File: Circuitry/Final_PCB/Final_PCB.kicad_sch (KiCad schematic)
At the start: 84 parts

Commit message: vacuum converter
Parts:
- C1, C2, C3, C4, C7: footprint Resistor_THT:R_Axial_DIN0204_L3.6mm_D1.6mm_P7.62mm_Horizontal -> Capacitor_THT:CP_Radial_D4.0mm_P2.00mm
- C5, C6: footprint Resistor_THT:R_Axial_DIN0207_L6.3mm_D2.5mm_P7.62mm_Horizontal -> Capacitor_THT:CP_Radial_D4.0mm_P2.00mm
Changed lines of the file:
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@@
       (effects (font (size 1.27 1.27)) (justify left) hide)
     )
-    (property "Footprint" "Resistor_THT:R_Axial_DIN0204_L3.6mm_D1.6mm_P7.62mm_Horizontal" (at 376.8852 172.72 0)
+    (property "Footprint" "Capacitor_THT:CP_Radial_D4.0mm_P2.00mm" (at 376.8852 172.72 0)
       (effects (font (size 1.27 1.27)) hide)
     )
@@
       (effects (font (size 1.27 1.27)) (justify left) hide)
     )
-    (property "Footprint" "Resistor_THT:R_Axial_DIN0204_L3.6mm_D1.6mm_P7.62mm_Horizontal" (at 378.1552 130.81 0)
+    (property "Footprint" "Capacitor_THT:CP_Radial_D4.0mm_P2.00mm" (at 378.1552 130.81 0)
       (effects (font (size 1.27 1.27)) hide)
     )
@@
       (effects (font (size 1.27 1.27)) (justify left) hide)
     )
-    (property "Footprint" "Resistor_THT:R_Axial_DIN0207_L6.3mm_D2.5mm_P7.62mm_Horizontal" (at 392.1252 172.72 0)
+    (property "Footprint" "Capacitor_THT:CP_Radial_D4.0mm_P2.00mm" (at 392.1252 172.72 0)
       (effects (font (size 1.27 1.27)) hide)
     )
@@
       (effects (font (size 1.27 1.27)) (justify left) hide)
     )
-    (property "Footprint" "Resistor_THT:R_Axial_DIN0207_L6.3mm_D2.5mm_P7.62mm_Horizontal" (at 408.6352 172.72 0)
+    (property "Footprint" "Capacitor_THT:CP_Radial_D4.0mm_P2.00mm" (at 408.6352 172.72 0)
       (effects (font (size 1.27 1.27)) hide)
     )
@@
       (effects (font (size 1.27 1.27)) (justify left) hide)
     )
-    (property "Footprint" "Resistor_THT:R_Axial_DIN0204_L3.6mm_D1.6mm_P7.62mm_Horizontal" (at 409.9052 130.81 0)
+    (property "Footprint" "Capacitor_THT:CP_Radial_D4.0mm_P2.00mm" (at 409.9052 130.81 0)
       (effects (font (size 1.27 1.27)) hide)
     )
@@
       (effects (font (size 1.27 1.27)) (justify left) hide)
     )
-    (property "Footprint" "Resistor_THT:R_Axial_DIN0204_L3.6mm_D1.6mm_P7.62mm_Horizontal" (at 393.3952 130.81 0)
+    (property "Footprint" "Capacitor_THT:CP_Radial_D4.0mm_P2.00mm" (at 393.3952 130.81 0)
       (effects (font (size 1.27 1.27)) hide)
     )
@@
     (in_bom yes) (on_board yes) (dnp no) (fields_autoplaced)
     (property "Reference" "C7" (at 396.24 212.09 0)
-      (effects (font (size 1.27 1.27)) (justify left))
+      (effects (font (size 1.27 1.27)) (justify left) hide)
     )
     (property "Value" "47 uF" (at 396.24 214.63 0)
-      (effects (font (size 1.27 1.27)) (justify left) hide)
-    )
-    (property "Footprint" "Resistor_THT:R_Axial_DIN0204_L3.6mm_D1.6mm_P7.62mm_Horizontal" (at 393.3952 217.17 0)
-      (effects (font (size 1.27 1.27)) hide)
-    )
+      (effects (font (size 1.27 1.27)) (justify left))
+    )
+    (property "Footprint" "Capacitor_THT:CP_Radial_D4.0mm_P2.00mm" (at 393.3952 217.17 0)
+      (effects (font (size 1.27 1.27)) hide)
+    )

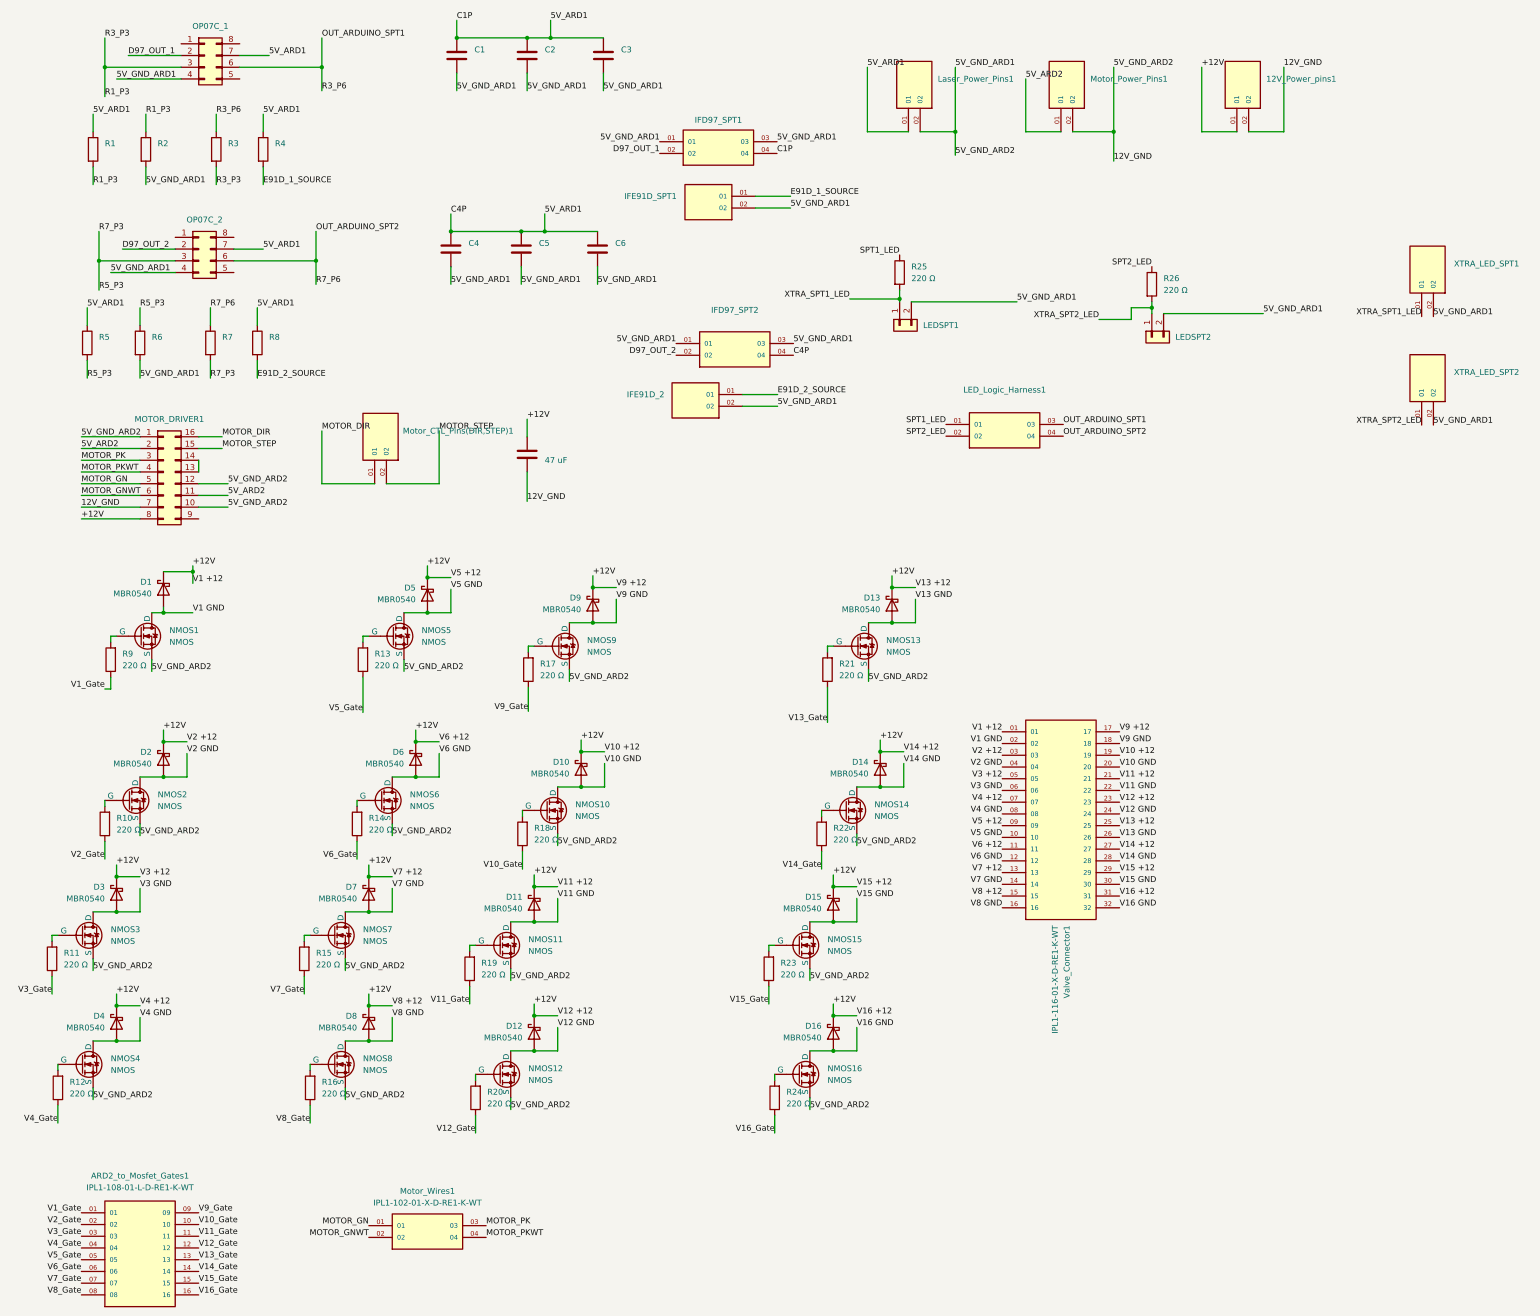
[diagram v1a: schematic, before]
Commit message: PCB minor correction/revision
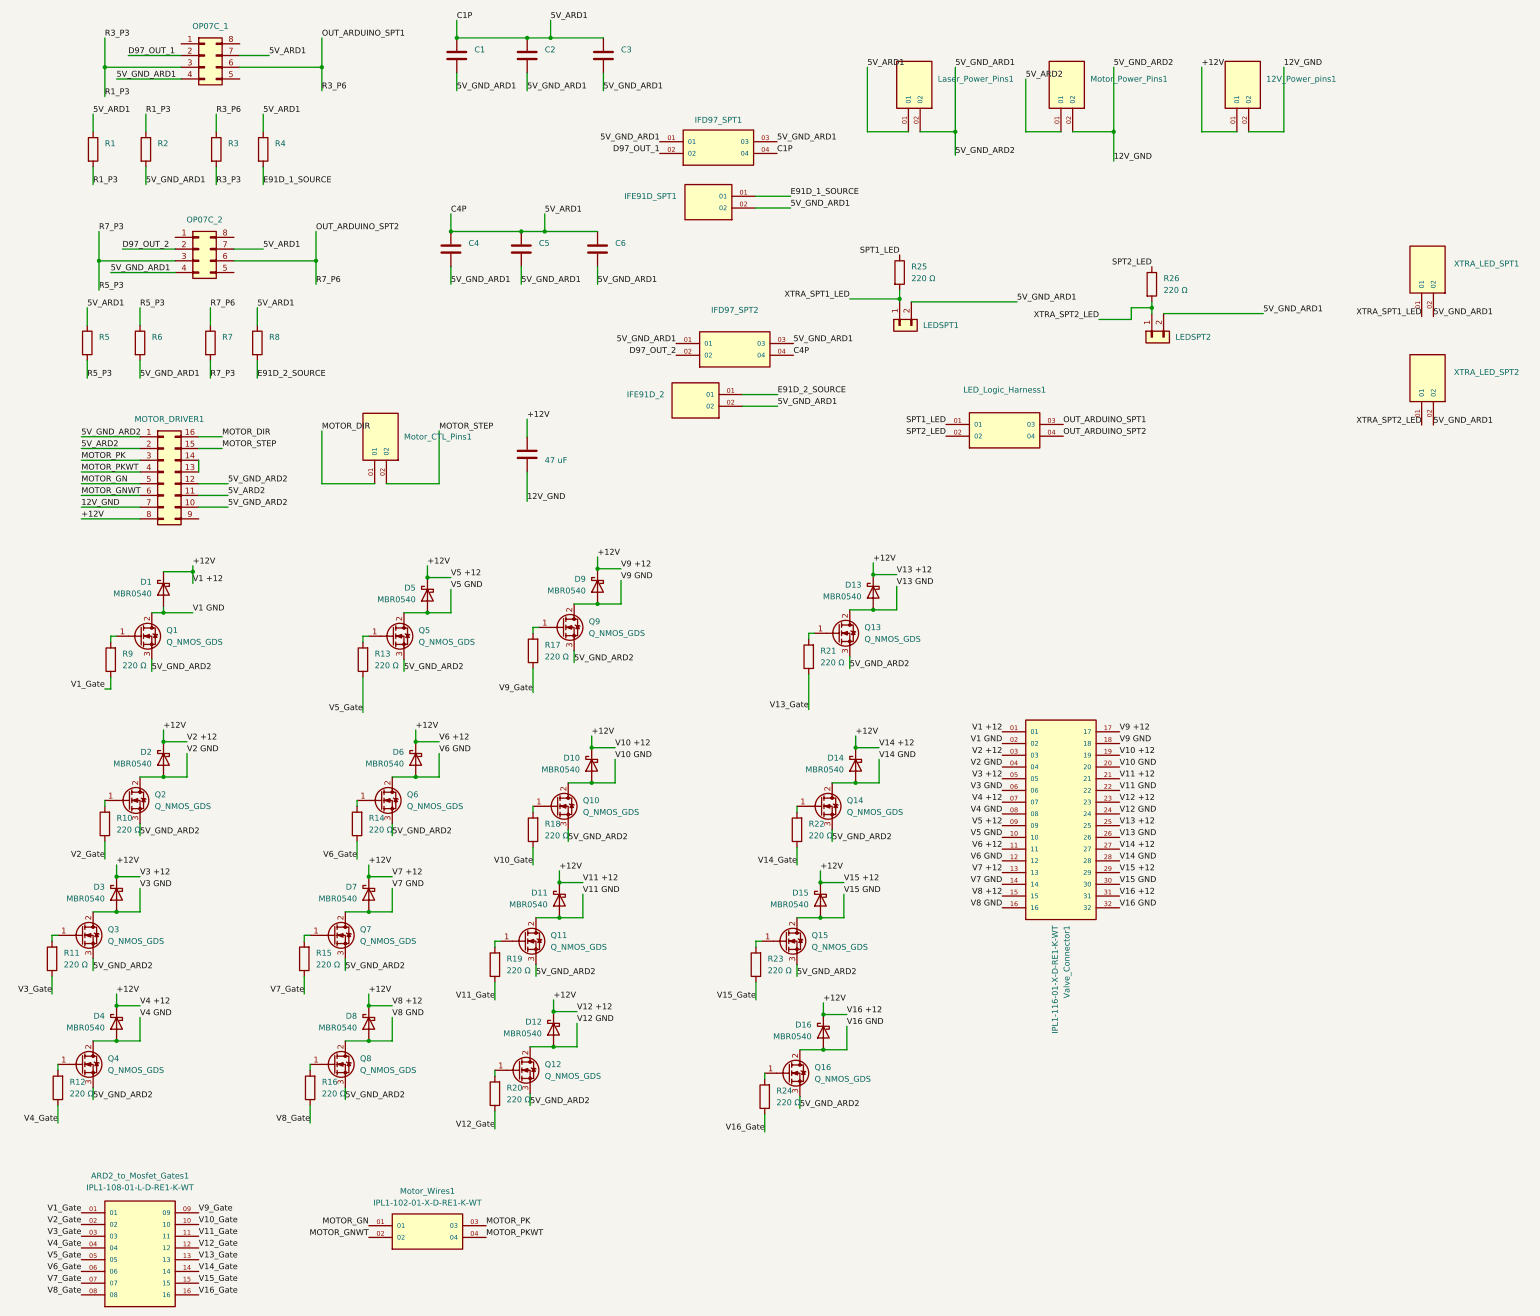
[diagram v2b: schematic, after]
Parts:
- removed NMOS1, NMOS10, NMOS11, NMOS12, NMOS13, NMOS14, NMOS15, NMOS16, NMOS2, NMOS3, NMOS4, NMOS5, NMOS6, NMOS7, NMOS8, NMOS9: NMOS, Final_PCB_Footprint:TO-220-3_Vertical, symbol Simulation_SPICE:NMOS
- added Q1, Q10, Q11, Q12, Q13, Q14, Q15, Q16, Q2, Q3, Q4, Q5, Q6, Q7, Q8, Q9: Q_NMOS_GDS, Final_PCB_Footprint:TO-220-3_Vertical, symbol Device:Q_NMOS_GDS
- renumbered Motor_CTL_Pins(DIR,STEP)1 to Motor_CTL_Pins1
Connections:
- net 12V_GND: now also Q1.3 (S), Q10.3 (S), Q11.3 (S), Q12.3 (S), Q13.3 (S), Q14.3 (S), Q15.3 (S), Q16.3 (S), Q2.3 (S), Q3.3 (S), Q4.3 (S), Q5.3 (S), Q6.3 (S), Q7.3 (S), Q8.3 (S), Q9.3 (S)
- net V1 GND: now also Q1.2 (D)
- net V10 GND: now also Q10.2 (D)
- net V11 GND: now also Q11.2 (D)
- net V12 GND: now also Q12.2 (D)
- net V13 GND: now also Q13.2 (D)
- net V14 GND: now also Q14.2 (D)
- net V15 GND: now also Q15.2 (D)
- net V16 GND: now also Q16.2 (D)
- net V2 GND: now also Q2.2 (D)
- net V3 GND: now also Q3.2 (D)
- net V4 GND: now also Q4.2 (D)
- net V5 GND: now also Q5.2 (D)
- net V6 GND: now also Q6.2 (D)
- net V7 GND: now also Q7.2 (D)
- net V8 GND: now also Q8.2 (D)
- net V9 GND: now also Q9.2 (D)
- net at R15.2: now also Q7.1 (G)
- net at R11.2: now also Q3.1 (G)
- net at R10.2: now also Q2.1 (G)
- net at R20.2: now also Q12.1 (G)
- net at R22.2: now also Q14.1 (G)
- net at R13.2: now also Q5.1 (G)
- net at R23.2: now also Q15.1 (G)
- net at R19.2: now also Q11.1 (G)
- net at R16.2: now also Q8.1 (G)
- net at R21.2: now also Q13.1 (G)
- net at R24.2: now also Q16.1 (G)
- net at R17.2: now also Q9.1 (G)
- net at R9.2: now also Q1.1 (G)
- net at R14.2: now also Q6.1 (G)
- net at R12.2: now also Q4.1 (G)
- net at R18.2: now also Q10.1 (G)
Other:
- moved on the sheet: D10, D11, D12, D13, D14, D15, D16, D9, R17, R18, R19, R20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

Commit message: Finishing touches PCB
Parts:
- C1, C3, C4, C6: footprint Capacitor_THT:CP_Radial_D4.0mm_P2.00mm -> Capacitor_THT:CP_Radial_D5.0mm_P2.00mm
- C2, C5: footprint Capacitor_THT:CP_Radial_D4.0mm_P2.00mm -> Capacitor_THT:CP_Radial_D10.0mm_P5.00mm
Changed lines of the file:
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@@
       (effects (font (size 1.27 1.27)) (justify left) hide)
     )
-    (property "Footprint" "Capacitor_THT:CP_Radial_D4.0mm_P2.00mm" (at 376.8852 172.72 0)
+    (property "Footprint" "Capacitor_THT:CP_Radial_D5.0mm_P2.00mm" (at 376.8852 172.72 0)
       (effects (font (size 1.27 1.27)) hide)
     )
@@
       (effects (font (size 1.27 1.27)) (justify left) hide)
     )
-    (property "Footprint" "Capacitor_THT:CP_Radial_D4.0mm_P2.00mm" (at 378.1552 130.81 0)
+    (property "Footprint" "Capacitor_THT:CP_Radial_D5.0mm_P2.00mm" (at 378.1552 130.81 0)
       (effects (font (size 1.27 1.27)) hide)
     )
@@
       (effects (font (size 1.27 1.27)) (justify left) hide)
     )
-    (property "Footprint" "Capacitor_THT:CP_Radial_D4.0mm_P2.00mm" (at 392.1252 172.72 0)
+    (property "Footprint" "Capacitor_THT:CP_Radial_D10.0mm_P5.00mm" (at 392.1252 172.72 0)
       (effects (font (size 1.27 1.27)) hide)
     )
@@
       (effects (font (size 1.27 1.27)) (justify left) hide)
     )
-    (property "Footprint" "Capacitor_THT:CP_Radial_D4.0mm_P2.00mm" (at 408.6352 172.72 0)
+    (property "Footprint" "Capacitor_THT:CP_Radial_D5.0mm_P2.00mm" (at 408.6352 172.72 0)
       (effects (font (size 1.27 1.27)) hide)
     )
@@
       (effects (font (size 1.27 1.27)) (justify left) hide)
     )
-    (property "Footprint" "Capacitor_THT:CP_Radial_D4.0mm_P2.00mm" (at 409.9052 130.81 0)
+    (property "Footprint" "Capacitor_THT:CP_Radial_D5.0mm_P2.00mm" (at 409.9052 130.81 0)
       (effects (font (size 1.27 1.27)) hide)
     )
@@
       (effects (font (size 1.27 1.27)) (justify left) hide)
     )
-    (property "Footprint" "Capacitor_THT:CP_Radial_D4.0mm_P2.00mm" (at 393.3952 130.81 0)
-      (effects (font (size 1.27 1.27)) hide)
-    )
+    (property "Footprint" "Capacitor_THT:CP_Radial_D10.0mm_P5.00mm" (at 393.3952 130.81 0)
+      (effects (font (size 1.27 1.27)) hide)
+    )
